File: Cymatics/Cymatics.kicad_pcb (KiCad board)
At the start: 2 copper layers, 65 x 70 mm, 79 parts, among them IC1 LMV358IDR, IC2 MAX7403CSA+, IC3 LMV358IDR, IC4 LMV358IDR, IC5 MAX7403CSA+, J1 Screw_Terminal_01x03, J10 Screw_Terminal_01x04, J11 Screw_Terminal_01x05, J12 Screw_Terminal_01x02, J13 Screw_Terminal_01x02, J14 RCU-0C, J15 Screw_Terminal_01x02, J16 Screw_Terminal_01x03, J17 Screw_Terminal_01x02, J18 Screw_Terminal_01x06, J19 RCU-0C, J2 Screw_Terminal_01x02, J20 RCU-0C, J21 RCU-0C, J22 RCU-0C, J23 RCU-0C, J24 RCU-0C, J3 Screw_Terminal_01x03, J4 Screw_Terminal_01x03, J5 Screw_Terminal_01x02, J6 Conn_01x16_Socket, J7 Conn_01x12_Socket, J8 Screw_Terminal_01x04, J9 Screw_Terminal_01x02, U1 SN74AHCT125DR, U2 MAX7480ESA+

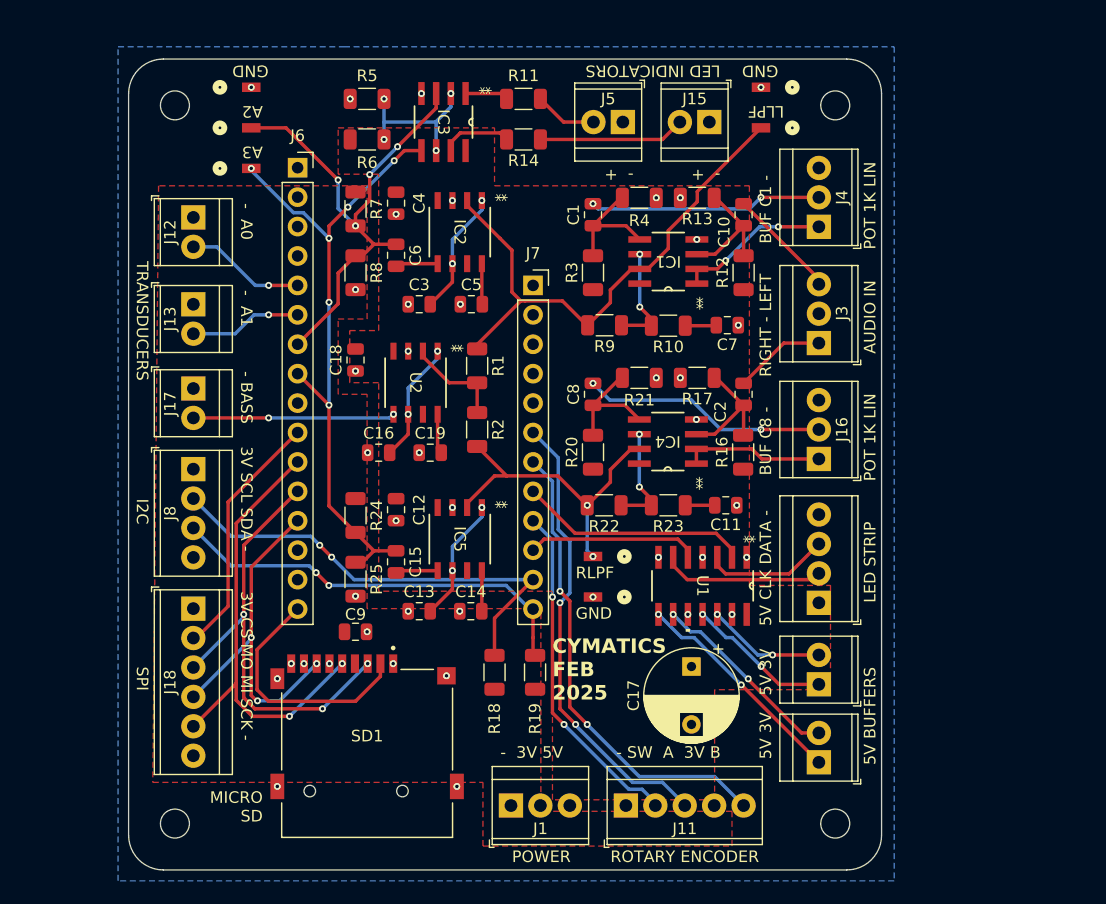
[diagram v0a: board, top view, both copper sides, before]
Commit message: pull up resistors for SPI and I2C
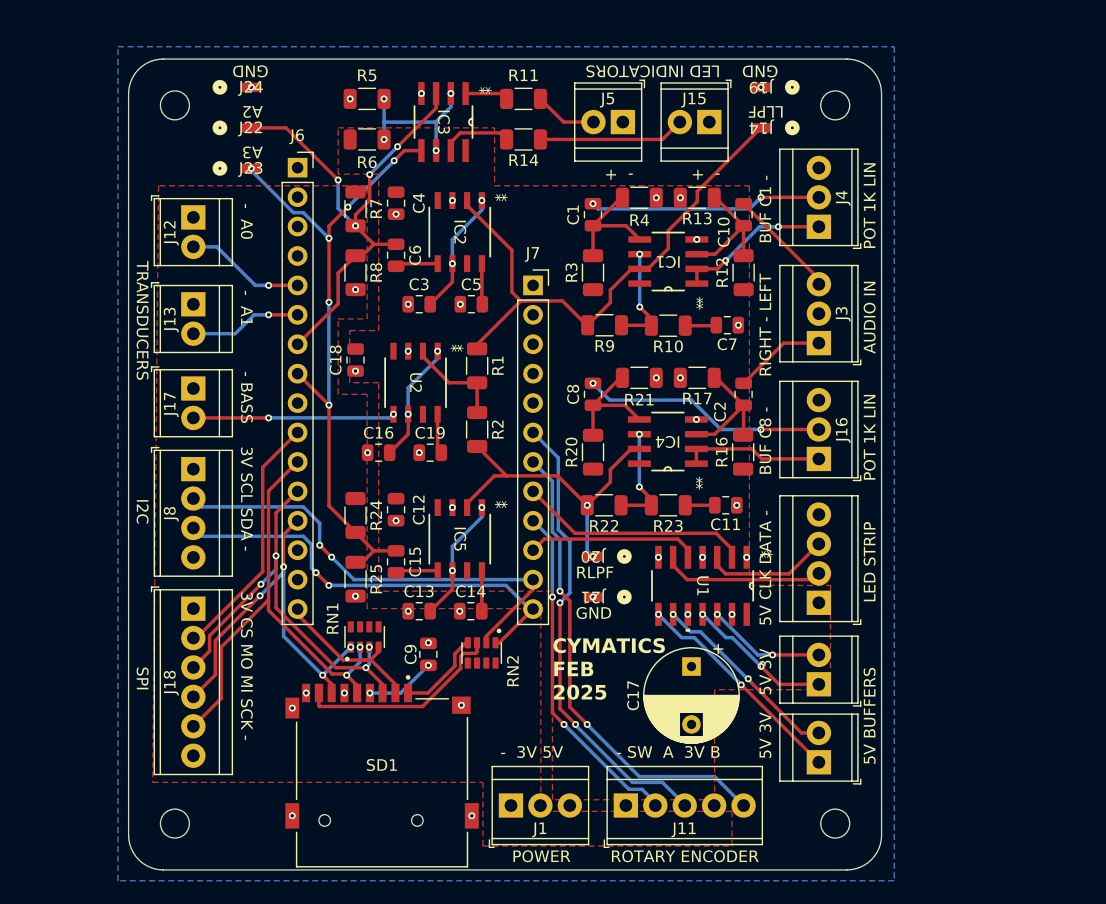
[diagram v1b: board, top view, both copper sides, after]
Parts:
- removed R18, R19: 10k, Resistor_SMD:R_1206_3216Metric
- added RN1: CAY16-473J4LF, CAY16:RESCAF80P320X160X60-8N, F.Cu at (110.5, 103.0)
- added RN2: CAY16-473J4LF, CAY16:RESCAF80P320X160X60-8N, F.Cu at (120.6, 104.4)
- moved C9 6.59 mm to (116.0, 104.5), turned to -90 degrees
- moved SD1 2.85 mm to (112.0, 115.6)
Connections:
- SD1 pad 1: GND -> DAT2
- SD1 pad 8: GND -> DAT1
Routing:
- net DAT1: track 0.00 -> 18.1 mm
- net DAT2: track 0.00 -> 7.57 mm
- net SD_CS: track 21.5 -> 14.1 mm
- net 3V3: track 0.00 -> 6.04 mm, vias 0 -> 2
- net MI: track 31.1 -> 35.0 mm, vias 3 -> 4
- net SCK: track 39.6 -> 41.3 mm
- net SDA: track 36.3 -> 37.9 mm
- net MO: track 38.8 -> 38.0 mm, vias 3 -> 4
- net GND: vias 41 -> 39
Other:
- board text removed: "MICRO SD"

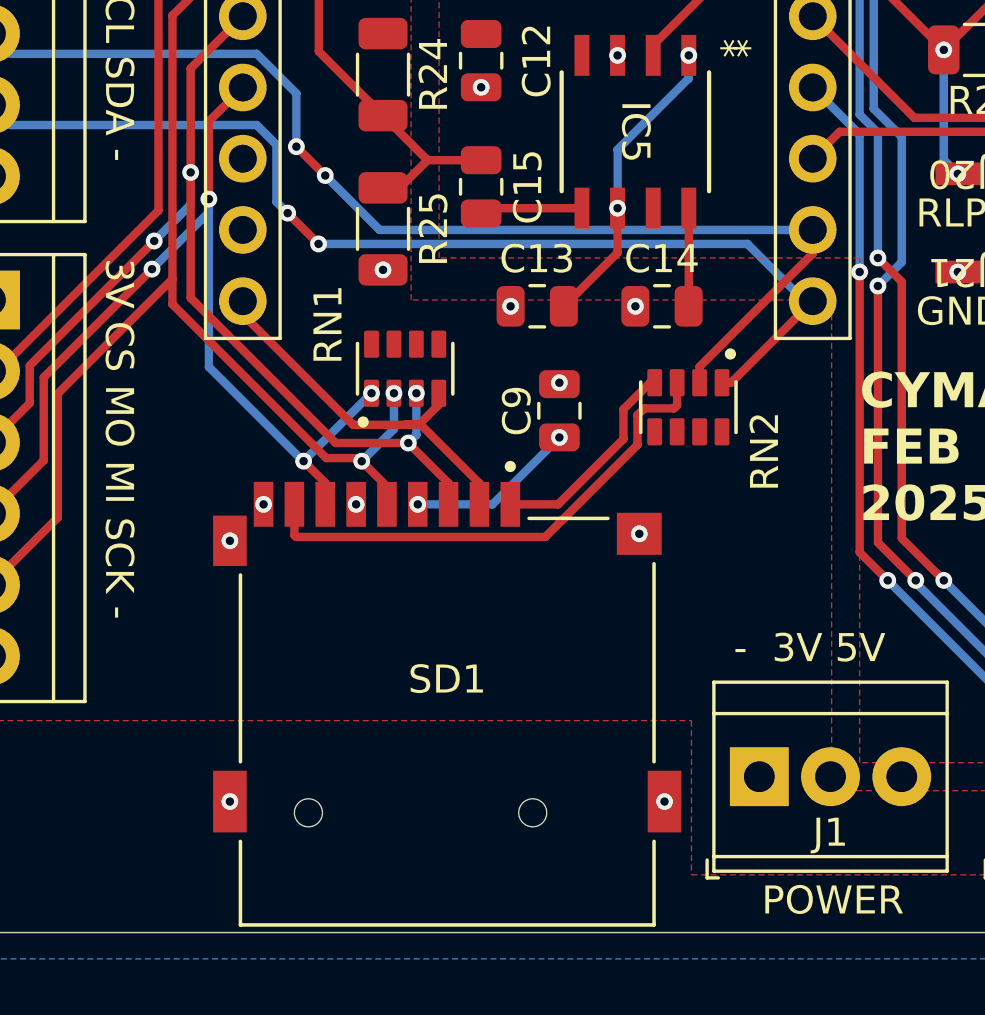
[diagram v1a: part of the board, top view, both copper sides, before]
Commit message: use 10k pullup for I2C and DAT1/2
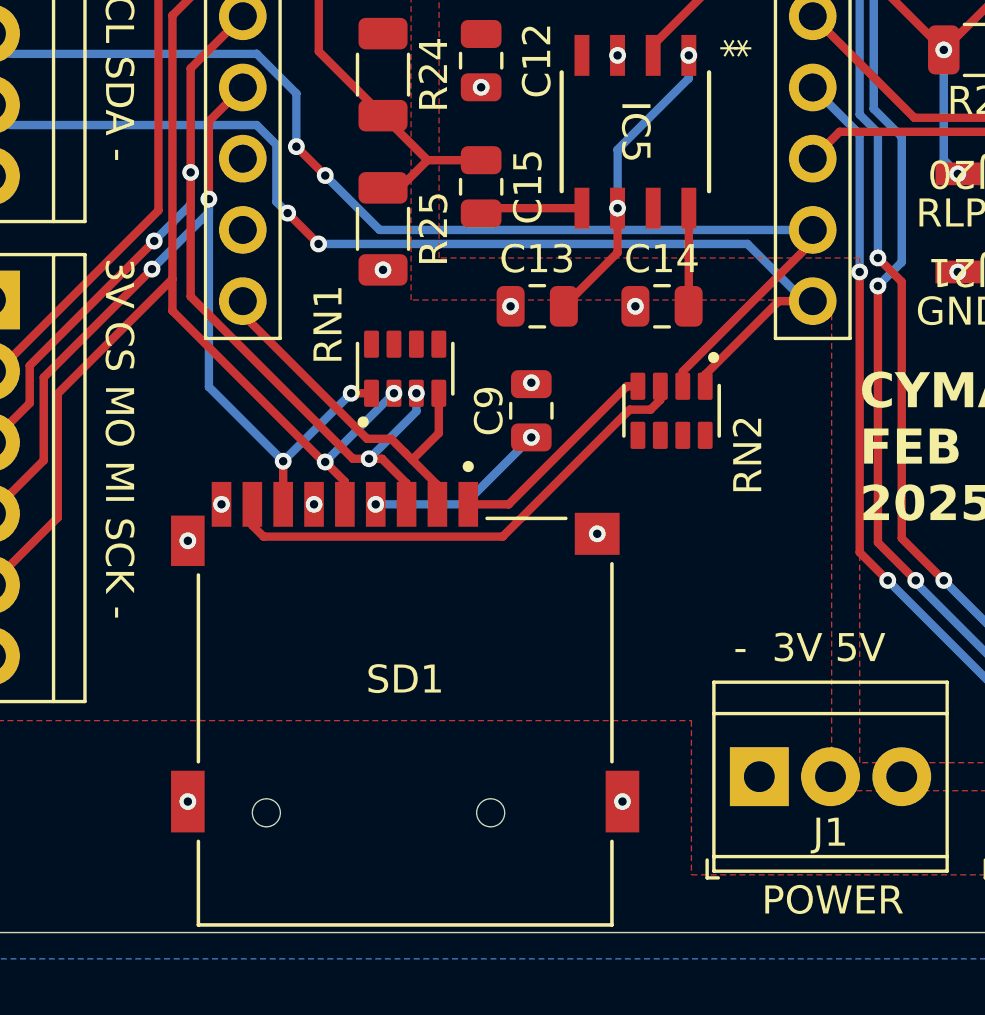
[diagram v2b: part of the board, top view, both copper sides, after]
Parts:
- RN2: value CAY16-473J4LF -> CAY16-103J4LF; footprint CAY16:RESCAF80P320X160X60-8N -> CAY16-103:RESCAF80P320X160X60-8N
- moved SD1 1.50 mm to (110.5, 115.6)
- moved C9 1.00 mm to (115.0, 104.5)
- moved RN2 0.61 mm to (120.0, 104.5)
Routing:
- net SDA: track 37.9 -> 38.8 mm
- net SCK: track 41.3 -> 40.6 mm
- net SD_CS: track 14.1 -> 13.4 mm
- net 3V3: track 6.04 -> 6.54 mm

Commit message: Order for March PCB
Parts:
- RN1: footprint CAY16:RESCAF80P320X160X60-8N -> CAY16-473:RESCAF80P320X160X60-8N
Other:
- board text added: "CYMATICS MAR 2025"
- board text removed: "CYMATICS FEB 2025"

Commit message: All changes up through Week 9, including making the step file
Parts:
- added C20: 10uF, Capacitor_SMD:C_0805_2012Metric, F.Cu at (103.0, 104.5)
- added RN3: CAY16-103J4LF, CAY16-103:RESCAF80P320X160X60-8N, F.Cu at (122.8, 109.5)
- RN2: value CAY16-103J4LF -> CAY16-473J4LF; footprint CAY16-103:RESCAF80P320X160X60-8N -> CAY16-473:RESCAF80P320X160X60-8N
- turned RN2 to 90 degrees
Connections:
- RN2 pad 1: SDA -> DAT2
- RN2 pad 2: SCL -> DAT1
- RN2 pad 3: DAT1 -> CD
- RN2 pad 4: DAT2 -> unconnected-(RN2-Pad4)
- RN2 pad 5: 3V3 -> unconnected-(RN2-Pad5)
- SD1 pad CD: GND -> CD
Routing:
- net CD: track 0.00 -> 19.5 mm
- net 3V3: track 6.54 -> 11.9 mm, vias 2 -> 3
- net SCL: track 40.8 -> 44.7 mm
- net SDA: track 38.8 -> 41.3 mm
- net DAT1: track 18.0 -> 17.2 mm
- net DAT2: track 7.79 -> 7.07 mm
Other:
- board text added: "CYMATICS MARCH 2025"
- board text removed: "CYMATICS MAR 2025"

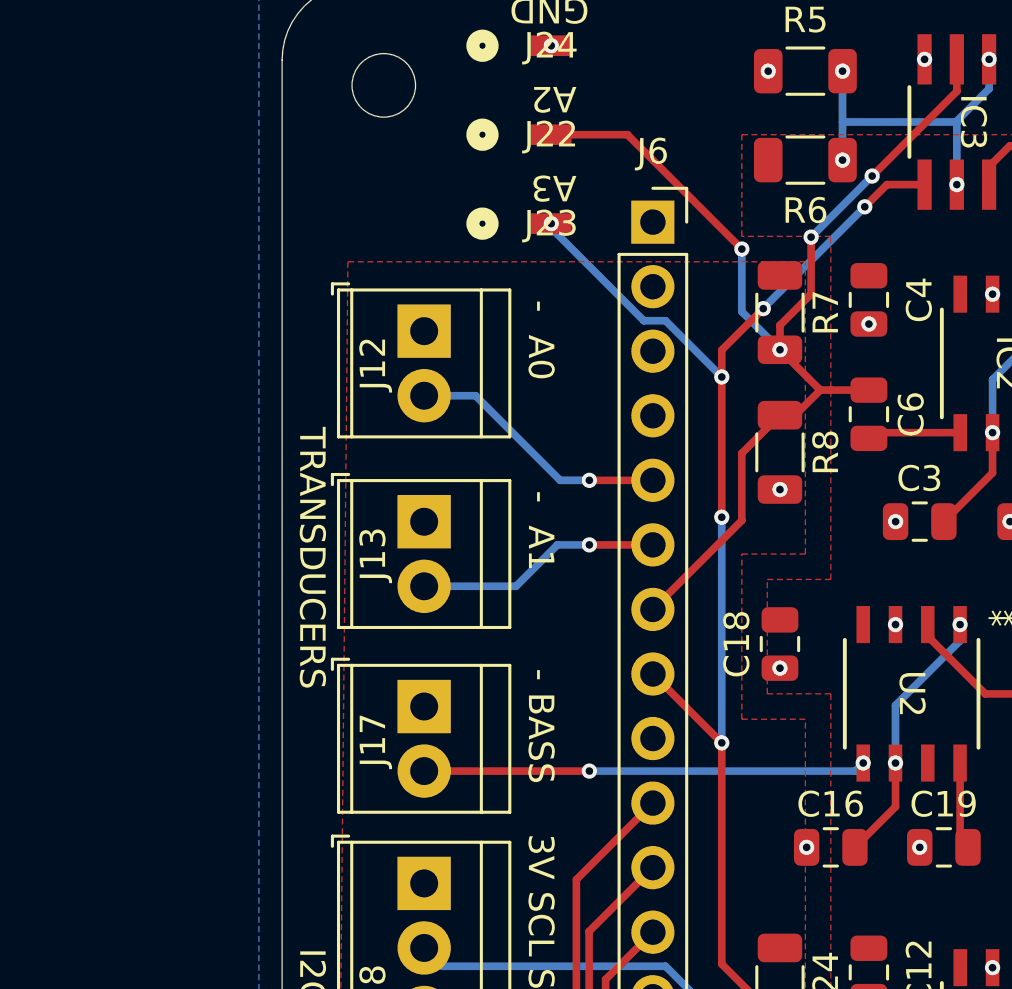
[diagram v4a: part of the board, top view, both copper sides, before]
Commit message: added passive DAC filters to schem and layout
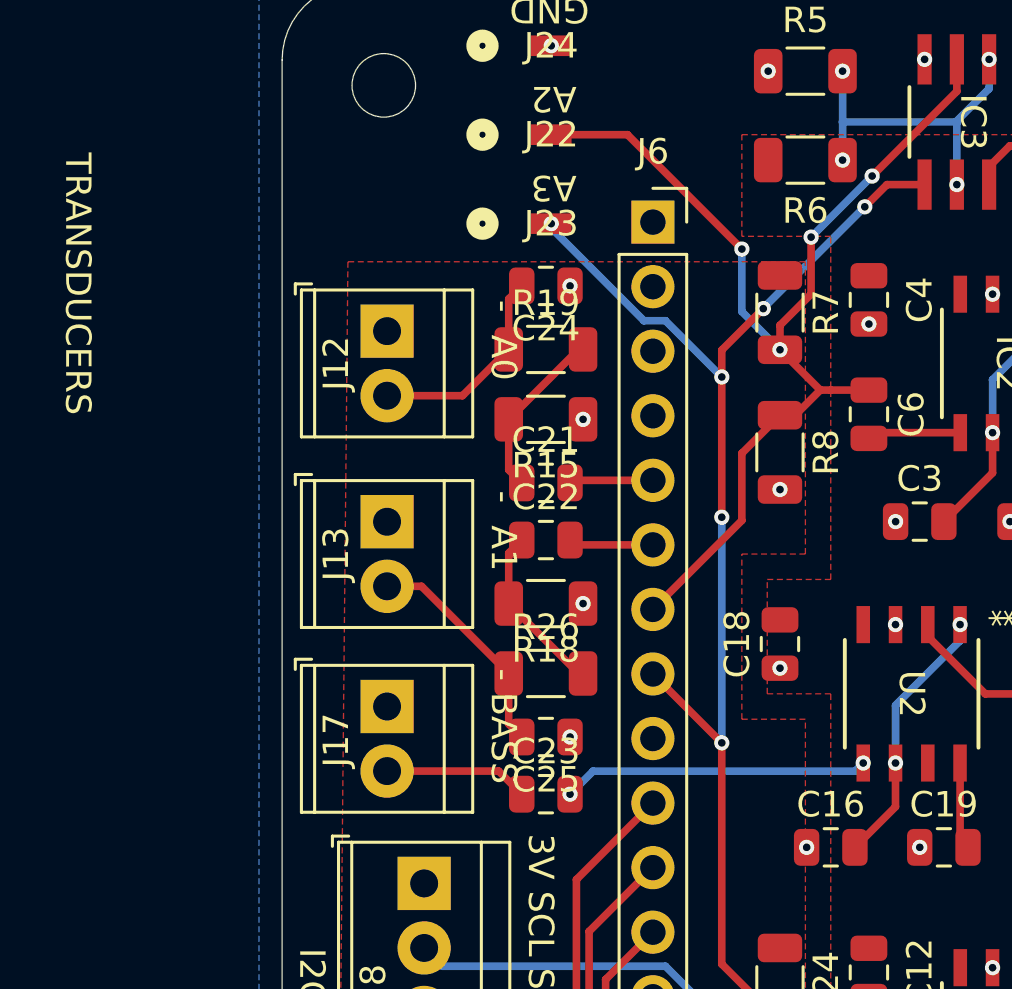
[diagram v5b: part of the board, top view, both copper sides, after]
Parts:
- added C21: 10uF, Capacitor_SMD:C_0805_2012Metric, F.Cu at (100.5, 72.8)
- added C22: 10uF, Capacitor_SMD:C_0805_2012Metric, F.Cu at (100.5, 75.0)
- added C23: 10uF, Capacitor_SMD:C_0805_2012Metric, F.Cu at (100.5, 85.0)
- added C24: 0.1uF, Capacitor_SMD:C_0805_2012Metric, F.Cu at (100.5, 65.0)
- added C25: 0.1uF, Capacitor_SMD:C_0805_2012Metric, F.Cu at (100.5, 82.8)
- added R15: 1.5k, Resistor_SMD:R_1206_3216Metric, F.Cu at (100.5, 70.2)
- added R18: 1.5k, Resistor_SMD:R_1206_3216Metric, F.Cu at (100.5, 77.5)
- added R19: 3.3k, Resistor_SMD:R_1206_3216Metric, F.Cu at (100.5, 67.5)
- added R26: 3.3k, Resistor_SMD:R_1206_3216Metric, F.Cu at (100.5, 80.2)
- moved J12 1.46 mm to (94.2, 66.8)
- moved J13 1.46 mm to (94.2, 74.3)
- moved J17 1.46 mm to (94.2, 81.5)
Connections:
- J12 pad 2: A0 -> Net-(J12-Pin_2)
- J13 pad 2: A1 -> Net-(J13-Pin_2)
- J17 pad 2: BASS_OUT -> Net-(J17-Pin_2)
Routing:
- net Net-(J13-Pin_2): track 0.00 -> 8.92 mm
- net Net-(J12-Pin_2): track 0.00 -> 8.25 mm
- net A0: track 10.4 -> 3.30 mm, vias 1 -> 0
- net Net-(C22-Pad1): track 0.00 -> 6.78 mm
- net Net-(C21-Pad1): track 0.00 -> 6.78 mm
- net A1: track 9.68 -> 3.34 mm, vias 1 -> 0
- net Net-(J17-Pin_2): track 0.00 -> 5.68 mm
- net BASS_OUT: track 17.4 -> 12.0 mm
- net GND: vias 39 -> 43

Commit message: misc updates
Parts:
- moved RN3 20.1 mm to (115.1, 91.0), turned to 0 degrees
- moved R15 17.2 mm to (116.8, 64.7), turned to -90 degrees
- moved C7 16.4 mm to (158.1, 74.0)
- moved J1 16.4 mm to (139.4, 115.5)
- moved J5 16.4 mm to (149.1, 56.5)
- moved REF** 16.4 mm to (167.4, 117.1)
- moved REF** 16.4 mm to (167.4, 55.1)
- moved U1 16.4 mm to (156.0, 96.5)
- moved C12 16.4 mm to (129.5, 90.0)
- moved C13 16.4 mm to (131.5, 98.7)
- moved C15 16.4 mm to (129.5, 94.5)
- moved C16 16.4 mm to (128.0, 85.1)
- moved C18 16.4 mm to (126.0, 77.1)
- moved C20 16.4 mm to (119.3, 102.5)
- moved C3 16.4 mm to (131.5, 72.2)
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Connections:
- RN3 pad 1: SDA -> SCL
- RN3 pad 2: SCL -> SDA
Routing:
- net SDA: track 41.3 -> 75.8 mm
- net SCL: track 44.7 -> 78.2 mm, vias 2 -> 1
- net EXT_CS: track 21.6 -> 28.2 mm
- net MO: track 37.6 -> 42.7 mm
- net A3: track 57.4 -> 61.7 mm
- net MI: track 35.1 -> 38.3 mm
- net A0: track 3.30 -> 5.75 mm
- net SCK: track 40.6 -> 43.0 mm
- net A1: track 3.34 -> 5.61 mm
- net Net-(J12-Pin_2): track 8.25 -> 10.3 mm
- net Net-(J17-Pin_2): track 5.68 -> 7.34 mm
- net BASS_OUT: track 12.0 -> 13.7 mm
- net USB: track 0.00 -> 1.55 mm
- net Net-(J13-Pin_2): track 8.92 -> 9.84 mm
- net A2: track 44.1 -> 44.8 mm
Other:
- board size 65 x 70 mm -> 70 x 70 mm
- board text added: "- 3V3 USB"
- board text added: "CYMATICS 03.21.25"
- board text added: "FILTERED HAPTICS"
- board text added: "OUT IN"
- board text removed: "- 3V 5V"
- board text removed: "5V 3V"
- board text removed: "CYMATICS MARCH 2025"
- board text removed: "TRANSDUCERS"
